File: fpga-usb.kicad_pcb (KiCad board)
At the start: 2 copper layers, 31.4 x 17.8 mm, 13 parts, among them J1 ZX62-B-5PA11, P1 CONN_6X2, U1 MAX3453EEUD

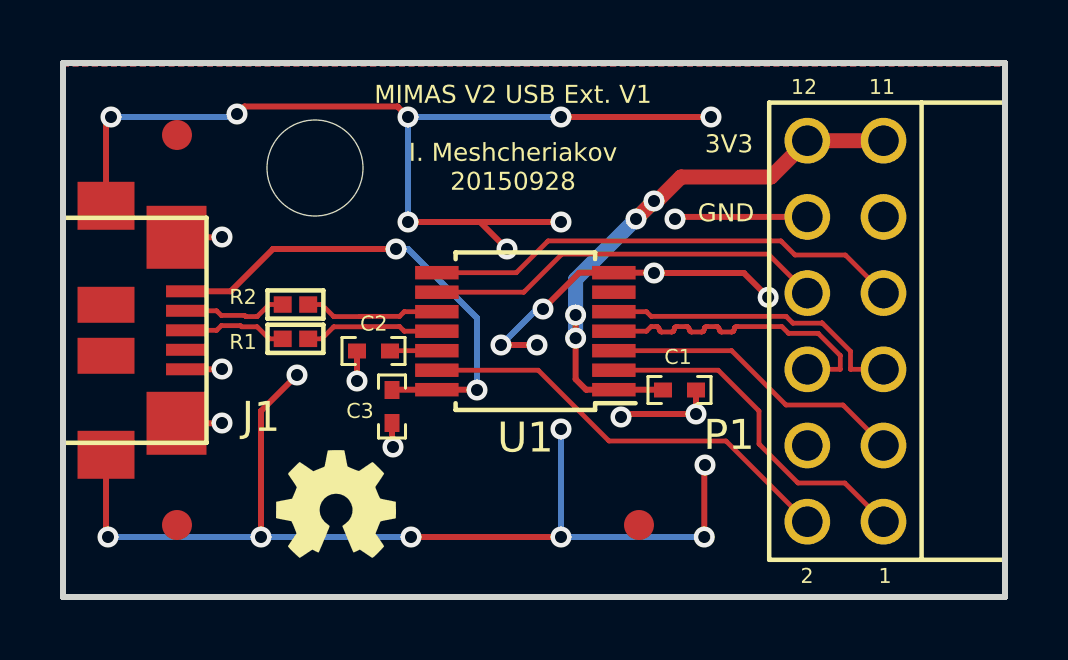
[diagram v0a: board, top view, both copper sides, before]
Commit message: Update text to indicate V2
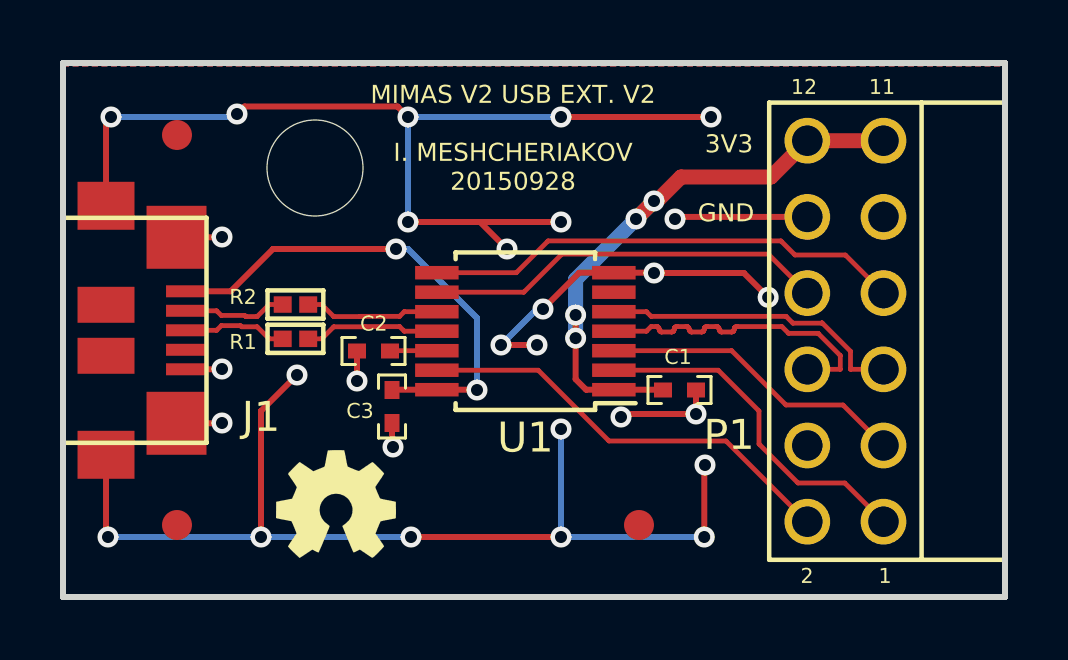
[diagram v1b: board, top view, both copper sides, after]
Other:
- board text added: "MIMAS V2 USB EXT. V2 I. MESHCHERIAKOV 20150928"
- board text removed: "MIMAS V2 USB Ext. V1 I. Meshcheriakov 20150928"
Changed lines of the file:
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@@
       (xy -1.21158 1.79578)) (layer F.SilkS) (width 0.00254))
   )
-  (gr_text "MIMAS V2 USB Ext. V1\n\nI. Meshcheriakov\n20150928" (at 146.4 97.7) (layer F.SilkS)
+  (gr_text "MIMAS V2 USB EXT. V2\n\nI. MESHCHERIAKOV\n20150928" (at 146.4 97.7) (layer F.SilkS)
     (effects (font (size 0.6 0.6) (thickness 0.15)))
   )

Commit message: Modify layout to use new part
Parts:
- removed FID** (x3): FIDUCIAL-1MM, usb:FIDUCIAL-1MM
- U1: value MAX3453EEUD -> MAX3453EETE; footprint Housings_SSOP:TSSOP-14_4.4x5mm_Pitch0.65mm -> Housings_DFN_QFN:QFN-16-1EP_3x3mm_Pitch0.5mm
- moved C1 6.55 mm to (145.5, 107.2), turned to 270 degrees
- moved C3 2.22 mm to (144.5, 107.2)
- moved U1 1.84 mm to (145.0, 103.8)
- moved C2 1.42 mm to (142.5, 106.0), turned to 270 degrees
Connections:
- U1 pad 1: +3.3V -> /ENUM
- U1 pad 2: /ENUM -> /RCV
- U1 pad 3: /RCV -> /V+
- U1 pad 4: /V+ -> /V-
- U1 pad 5: /V- -> (no net)
- U1 pad 6: (no net) -> GND
- U1 pad 7: GND -> /SUS
- U1 pad 8: /SUS -> (no net)
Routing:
- net /V+: track 10.2 -> 14.3 mm
- net /V-: track 10.1 -> 13.8 mm
- net /RCV: track 10.3 -> 13.9 mm
- net /BD: track 14.4 -> 17.8 mm
- net /ENUM: track 11.7 -> 14.7 mm
- net /~OE: track 13.4 -> 15.4 mm
- net /USB_VBUS: track 16.5 -> 14.7 mm
- net GND: track 96.5 -> 94.8 mm, vias 29 -> 26
- net /SUS: track 16.0 -> 17.1 mm
- net +3.3V: track 20.9 -> 20.1 mm, vias 4 -> 2
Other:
- net class Power: clearance 0.2 -> 0.16
- board text added: "MIMAS V2 USB EXT. V3 I. MESHCHERIAKOV 20151102"
- board text removed: "MIMAS V2 USB EXT. V2 I. MESHCHERIAKOV 20150928"
